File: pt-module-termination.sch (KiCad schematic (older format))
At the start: 2 parts

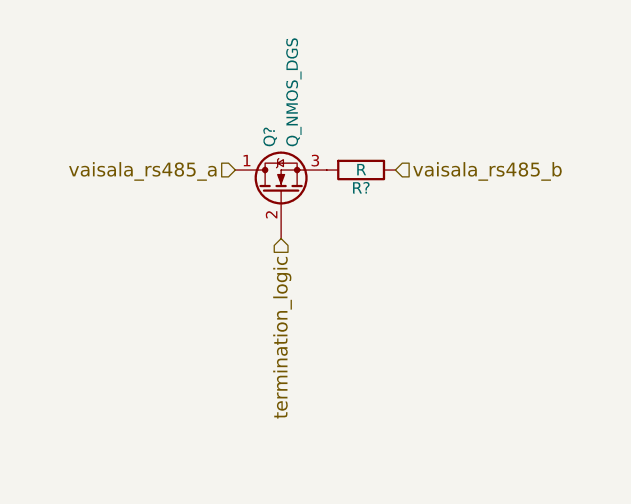
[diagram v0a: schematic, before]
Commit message: add resistor values
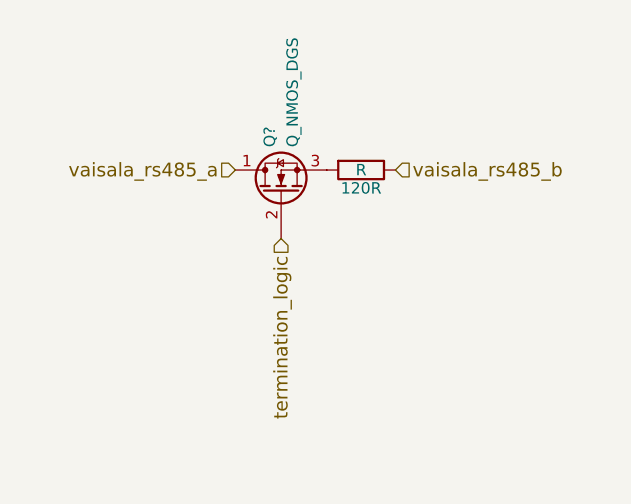
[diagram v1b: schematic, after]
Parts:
- gave numbers to parts that had none: 1
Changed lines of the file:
@@
 $EndComp
 $Comp
-L R R?
+L R 120R
 U 1 1 5987C0FF
 P 3750 2350
-F 0 "R?" V 3830 2350 50  0000 C CNN
+F 0 "120R" V 3830 2350 50  0000 C CNN
 F 1 "R" V 3750 2350 50  0000 C CNN
 F 2 "" V 3680 2350 50  0001 C CNN

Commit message: Added resistor and capacitor values in MCU sheet.
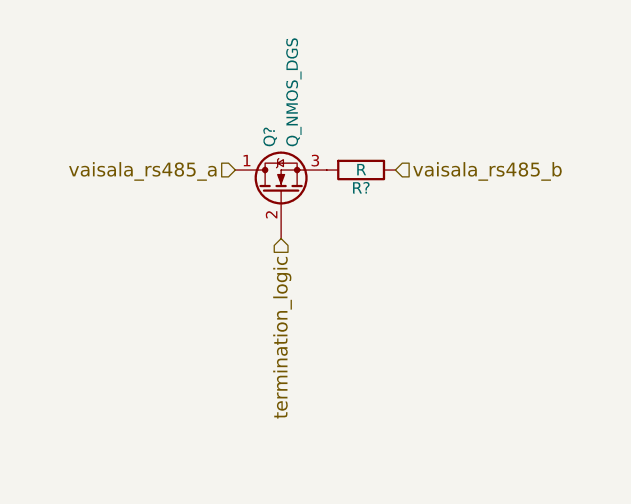
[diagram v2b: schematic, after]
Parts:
- renumbered 120R to R?
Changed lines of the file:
@@
 $EndComp
 $Comp
-L R 120R
+L R R?
 U 1 1 5987C0FF
 P 3750 2350
-F 0 "120R" V 3830 2350 50  0000 C CNN
+F 0 "R?" V 3830 2350 50  0000 C CNN
 F 1 "R" V 3750 2350 50  0000 C CNN
 F 2 "" V 3680 2350 50  0001 C CNN
